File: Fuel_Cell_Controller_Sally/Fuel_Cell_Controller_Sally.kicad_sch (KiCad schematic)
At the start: 87 parts, among them J1 STM32-Prog-Header, J4 USB_C_Receptacle_USB2.0_14P, J6 OLED, Q1 SI2302A-TPMSCT-ND, Q2 SI2302A-TPMSCT-ND, SW1 PTS815 SJM 250 SMTR LFS, SW2 PTS815 SJM 250 SMTR LFS, U1 TPS259631, U2 AZ1117IH-3.3, U20 STM32G491CETx, U3 TPS565208, U4 TPS259631, U8 MCP6007, U9 USBLC6-2SC6, X2 OXETDLJANF-8MHZ

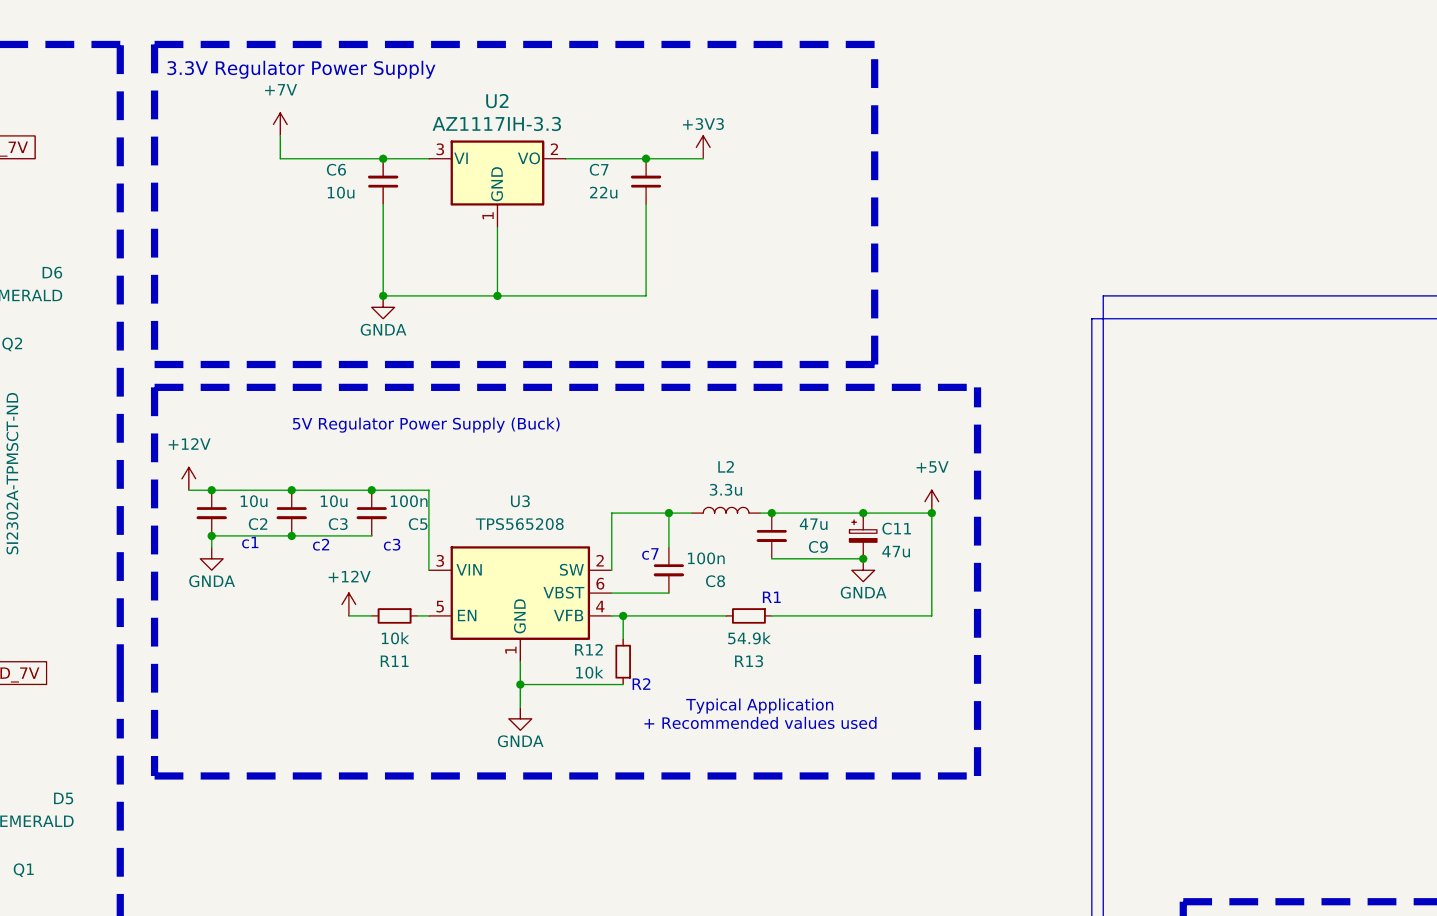
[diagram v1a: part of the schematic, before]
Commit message: FC con, power layout
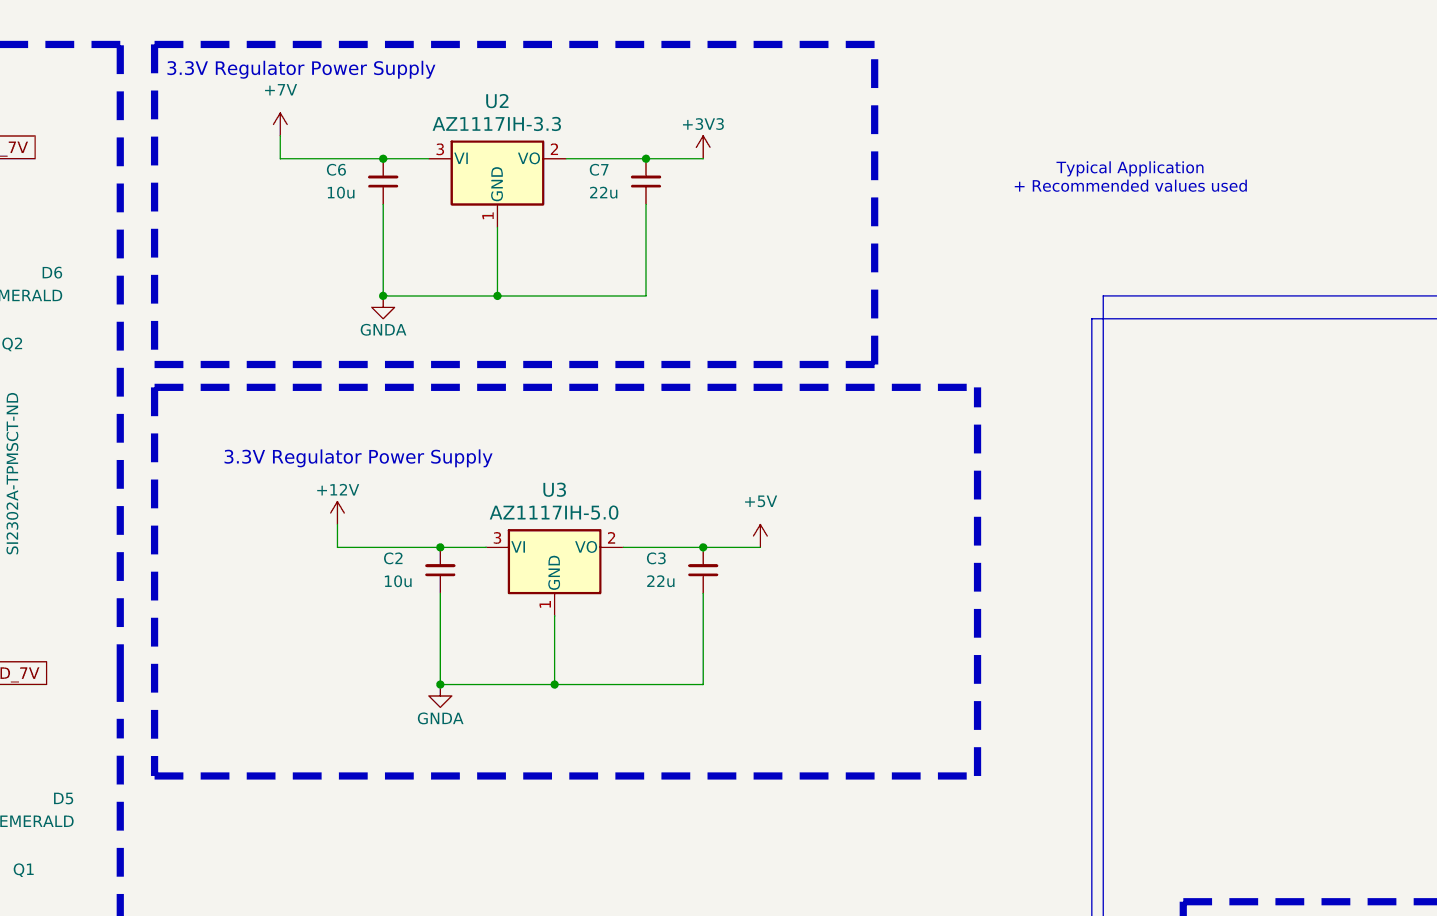
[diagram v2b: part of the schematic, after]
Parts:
- removed C11: 47u, Capacitor_SMD:CP_Elec_4x5.4, symbol Device:C_Polarized_Small
- removed C5, C8: 100n, Capacitor_SMD:C_0603_1608Metric, symbol Device:C_Small
- removed C9: 47u, Capacitor_SMD:C_0603_1608Metric, symbol Device:C_Small
- removed L2: 3.3u, Inductor_SMD:L_0805_2012Metric, symbol Device:L
- removed R11, R12: 10k, Resistor_SMD:R_0603_1608Metric, symbol Device:R_Small
- removed R13: 54.9k, Resistor_SMD:R_0603_1608Metric, symbol Device:R_Small
- removed U3: TPS565208, Package_TO_SOT_SMD:SOT-23-6, symbol Regulator_Switching:TPS565208
- added U3: AZ1117IH-5.0, Package_TO_SOT_SMD:SOT-223-3_TabPin2, symbol ecocad_lib_symbols:AZ1117IH-5.0
- C2: Part# C14663 -> C15849
- C3: value 10u -> 22u; Part# C14663 -> C15849
- X2: value OXETDLJANF-8MHZ -> OXETDLJANF-8MHZ
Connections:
- net +12V: now also C2.2, U3.3 (VI); no longer C2.1, C3.1
- net +5V: now also C3.2, U3.2 (VO)
- net GNDA: now also C2.1, C3.1, U3.1 (GND); no longer C2.2, C3.2
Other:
- note removed: "5V Regulator Power Supply (Buck)"
- note removed: "R1"
- note removed: "R2"
- note removed: "c1"
- note removed: "c2"
- note removed: "c3"
- note removed: "c7"

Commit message: MCU pinout layout in progress
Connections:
- net +3.3V is gone; now on net +3V3: C9.1, RV1.3, RV2.3, X2.1 (Tri-State), X2.4 (VDD)
- net BOOT0: no longer J6.3 (Pin_3), R25.1, U20.39 (PA15)
- new net I2C_{SCL}: J6.3 (Pin_3), R25.1, U20.39 (PA15)
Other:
- moved on the sheet: J4, U9
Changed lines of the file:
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@@
 	)
 	(junction
-		(at 252.73 182.88)
+		(at 245.11 182.88)
 		(diameter 0)
 		(color 0 0 0 0)
@@
 	)
 	(junction
-		(at 252.73 180.34)
+		(at 245.11 180.34)
 		(diameter 0)
 		(color 0 0 0 0)
 	)
 	(junction
-		(at 269.24 205.74)
+		(at 261.62 205.74)
 		(diameter 0)
 		(color 0 0 0 0)
@@
 	)
 	(no_connect
-		(at 254 170.18)
+		(at 246.38 170.18)
 	)
 	(no_connect
@@
 	)
 	(no_connect
-		(at 254 172.72)
+		(at 246.38 172.72)
 	)
 	(no_connect
@@
 	(wire
 		(pts
-			(xy 252.73 182.88) (xy 254 182.88)
+			(xy 245.11 182.88) (xy 246.38 182.88)
 		)
 		(stroke
@@
 	(wire
 		(pts
-			(xy 246.38 165.1) (xy 246.38 175.26)
+			(xy 238.76 165.1) (xy 238.76 175.26)
 		)
 		(stroke
@@
 	(wire
 		(pts
-			(xy 252.73 185.42) (xy 254 185.42)
+			(xy 245.11 185.42) (xy 246.38 185.42)
 		)
 		(stroke
@@
 	(wire
 		(pts
-			(xy 252.73 180.34) (xy 254 180.34)
+			(xy 245.11 180.34) (xy 246.38 180.34)
 		)
 		(stroke
@@
 	(wire
 		(pts
-			(xy 276.86 205.74) (xy 276.86 203.2)
+			(xy 269.24 205.74) (xy 269.24 203.2)
 		)
 		(stroke
@@
 	(wire
 		(pts
-			(xy 251.46 180.34) (xy 252.73 180.34)
+			(xy 243.84 180.34) (xy 245.11 180.34)
 		)
 		(stroke
@@
 	(wire
 		(pts
-			(xy 254 165.1) (xy 246.38 165.1)
+			(xy 246.38 165.1) (xy 238.76 165.1)
 		)
 		(stroke
@@
 	(wire
 		(pts
-			(xy 233.68 180.34) (xy 241.3 180.34)
+			(xy 226.06 180.34) (xy 233.68 180.34)
 		)
 		(stroke
@@
 	(wire
 		(pts
-			(xy 251.46 182.88) (xy 252.73 182.88)
+			(xy 243.84 182.88) (xy 245.11 182.88)
 		)
 		(stroke
@@
 	(wire
 		(pts
-			(xy 252.73 177.8) (xy 254 177.8)
+			(xy 245.11 177.8) (xy 246.38 177.8)
 		)
 		(stroke
@@
 	(wire
 		(pts
-			(xy 246.38 187.96) (xy 246.38 205.74)
+			(xy 238.76 187.96) (xy 238.76 205.74)
 		)
 		(stroke
@@
 	(wire
 		(pts
-			(xy 269.24 203.2) (xy 269.24 205.74)
+			(xy 261.62 203.2) (xy 261.62 205.74)
 		)
 		(stroke
@@
 	(wire
 		(pts
-			(xy 269.24 205.74) (xy 276.86 205.74)
+			(xy 261.62 205.74) (xy 269.24 205.74)
 		)
 		(stroke
@@
 	(wire
 		(pts
-			(xy 233.68 182.88) (xy 241.3 182.88)
+			(xy 226.06 182.88) (xy 233.68 182.88)
 		)
 		(stroke
@@
 	(wire
 		(pts
-			(xy 252.73 182.88) (xy 252.73 185.42)
+			(xy 245.11 182.88) (xy 245.11 185.42)
 		)
 		(stroke
@@
 	(wire
 		(pts
-			(xy 269.24 205.74) (xy 269.24 208.28)
+			(xy 261.62 205.74) (xy 261.62 208.28)
 		)
 		(stroke
@@
 	(wire
 		(pts
-			(xy 252.73 180.34) (xy 252.73 177.8)
+			(xy 245.11 180.34) (xy 245.11 177.8)
 		)
 		(stroke
@@
 	(wire
 		(pts
-			(xy 246.38 205.74) (xy 269.24 205.74)
+			(xy 238.76 205.74) (xy 261.62 205.74)
 		)
 		(stroke
@@
 	)
 	(rectangle
-		(start 228.6 154.94)
-		(end 312.42 214.63)
+		(start 220.98 154.94)
+		(end 304.8 214.63)
 		(stroke
 			(width 0.7874)
@@
 	(text "USB C\n"
 		(exclude_from_sim no)
-		(at 232.41 159.258 0)
+		(at 224.79 159.258 0)
 		(effects
 			(font
@@
 	)
 	(label "USB_{DP}"
-		(at 233.68 182.88 0)
+		(at 226.06 182.88 0)
 		(fields_autoplaced yes)
 		(effects
@@
 	)
 	(label "USB_{DM}"
-		(at 233.68 180.34 0)
+		(at 226.06 180.34 0)
 		(fields_autoplaced yes)
 		(effects
@@
 	)
 	(label "VBUS"
-		(at 246.38 165.1 0)
+		(at 238.76 165.1 0)
 		(fields_autoplaced yes)
 		(effects
@@
 		)
 	)
-	(label "PB8"
+	(label "PA15"
 		(at 379.73 233.68 0)
 		(fields_autoplaced yes)
@@
 			)
 		)
-		(property "Value" "+3.3V"
+		(property "Value" "+3V3"
 			(at 288.29 121.92 0)
 			(effects
@@
 	(symbol
 		(lib_id "power:GNDA")
-		(at 269.24 208.28 0)
+		(at 261.62 208.28 0)
 		(unit 1)
 		(exclude_from_sim no)
@@
 		(fields_autoplaced yes)
 		(property "Reference" "#PWR046"
-			(at 269.24 214.63 0)
+			(at 261.62 214.63 0)
 			(effects
 				(font
@@
 		)
 		(property "Value" "GNDA"
-			(at 269.24 213.36 0)
+			(at 261.62 213.36 0)
 			(effects
 				(font
@@
 		)
 		(property "Footprint" ""
-			(at 269.24 208.28 0)
+			(at 261.62 208.28 0)
 			(effects
 				(font
@@
 		)
 		(property "Datasheet" ""
-			(at 269.24 208.28 0)
+			(at 261.62 208.28 0)
 			(effects
 				(font
@@
 		)
 		(property "Description" ""
-			(at 269.24 208.28 0)
+			(at 261.62 208.28 0)
 			(effects
 				(font
@@
 			)
 		)
-		(property "Value" "+3.3V"
+		(property "Value" "+3V3"
 			(at 320.04 121.92 0)
 			(effects
@@
 	)
 	(symbol
+		(lib_id "power:+3V3")
+		(at 34.29 166.37 0)
+		(unit 1)
+		(exclude_from_sim no)
+		(in_bom yes)
+		(on_board yes)
+		(dnp no)
+		(fields_autoplaced yes)
+		(property "Reference" "#PWR026"
+			(at 34.29 170.18 0)
+			(effects
+				(font
+					(size 1.27 1.27)
+				)
+				(hide yes)
+			)
+		)
+		(property "Value" "+3V3"
+			(at 34.29 162.56 0)
+			(effects
+				(font
+					(size 1.27 1.27)
+				)
+			)
+		)
+		(property "Footprint" ""
+			(at 34.29 166.37 0)
+			(effects
+				(font
+					(size 1.27 1.27)
+				)
+				(hide yes)
+			)
+		)
+		(property "Datasheet" ""
+			(at 34.29 166.37 0)
+			(effects
+				(font
+					(size 1.27 1.27)
+				)
+				(hide yes)
+			)
+		)
+		(property "Description" ""
+			(at 34.29 166.37 0)
+			(effects
+				(font
+					(size 1.27 1.27)
+				)
+				(hide yes)
+			)
+		)
+		(pin "1"
+		)
+		(instances
+			(project "Fuel_Cell_Controller_Sally"
+				(path "/f651cec9-411c-4a4e-a163-5c49adbe6a12"
+					(reference "#PWR026")
+					(unit 1)
+				)
+			)
+		)
+	)
+	(symbol
 		(lib_id "power:GNDA")
 		(at 198.12 200.66 0)
@@
 	(symbol
 		(lib_id "Connector:USB_C_Receptacle_USB2.0_14P")
-		(at 269.24 180.34 0)
+		(at 261.62 180.34 0)
 		(mirror y)
 		(unit 1)
@@
 		(fields_autoplaced yes)
 		(property "Reference" "J4"
-			(at 280.67 179.0699 0)
+			(at 273.05 179.0699 0)
 			(effects
 				(font
@@
 		)
 		(property "Value" "USB_C_Receptacle_USB2.0_14P"
-			(at 280.67 181.6099 0)
+			(at 273.05 181.6099 0)
 			(effects
 				(font
@@
 		)
 		(property "Footprint" "Connector_USB:USB_C_Receptacle_GCT_USB4105-xx-A_16P_TopMnt_Horizontal"
-			(at 265.43 180.34 0)
+			(at 257.81 180.34 0)
 			(effects
 				(font
@@
 		)
 		(property "Datasheet" "https://www.usb.org/sites/default/files/documents/usb_type-c.zip"
-			(at 265.43 180.34 0)
+			(at 257.81 180.34 0)
 			(effects
 				(font
@@
 		)
 		(property "Description" "USB 2.0-only 14P Type-C Receptacle connector"
-			(at 269.24 180.34 0)
+			(at 261.62 180.34 0)
 			(effects
 				(font
@@
 	(symbol
 		(lib_id "Power_Protection:USBLC6-2SC6")
-		(at 246.38 180.34 0)
+		(at 238.76 180.34 0)
 		(mirror y)
 		(unit 1)
@@
 		(dnp no)
 		(property "Reference" "U9"
-			(at 244.7289 172.72 0)
+			(at 237.1089 172.72 0)
 			(effects
 				(font
@@
 		)
 		(property "Value" "USBLC6-2SC6"
-			(at 244.7289 175.26 0)
+			(at 237.1089 175.26 0)
 			(effects
 				(font
@@
 		)
 		(property "Footprint" "Package_TO_SOT_SMD:SOT-23-6"
-			(at 245.11 186.69 0)
+			(at 237.49 186.69 0)
 			(effects
 				(font
@@
 		)
 		(property "Datasheet" "https://www.st.com/resource/en/datasheet/usblc6-2.pdf"
-			(at 245.11 188.595 0)
+			(at 237.49 188.595 0)
 			(effects
 				(font
@@
 		)
 		(property "Description" "Very low capacitance ESD protection diode, 2 data-line, SOT-23-6"
-			(at 246.38 180.34 0)
+			(at 238.76 180.34 0)
 			(effects
 				(font
@@
 					(unit 1)
 				)
-			)
-		)
-	)
-	(symbol
-		(lib_id "power:+3.3V")
-		(at 34.29 166.37 0)
-		(unit 1)
-		(exclude_from_sim no)
-		(in_bom yes)
-		(on_board yes)
-		(dnp no)
-		(fields_autoplaced yes)
-		(property "Reference" "#PWR0118"
-			(at 34.29 170.18 0)
-			(effects
-				(font
-					(size 1.27 1.27)
-				)
-				(hide yes)
-			)
-		)
-		(property "Value" "+3.3V"
-			(at 34.29 161.29 0)
-			(effects
-				(font
-					(size 1.27 1.27)
-				)
-			)
-		)
-		(property "Footprint" ""
-			(at 34.29 166.37 0)
-			(effects
-				(font
-					(size 1.27 1.27)
-				)
-				(hide yes)
-			)
-		)
-		(property "Datasheet" ""
-			(at 34.29 166.37 0)
-			(effects
-				(font
-					(size 1.27 1.27)
-				)
-				(hide yes)
-			)
-		)
-		(property "Description" "Power symbol creates a global label with name \"+3.3V\""
-			(at 34.29 166.37 0)
-			(effects
-				(font
-					(size 1.27 1.27)
-				)
-				(hide yes)
-			)
-		)
-		(pin "1"
-		)
-		(instances
-			(project "Fuel_Cell_Controller_Prototype"
-				(path "/f651cec9-411c-4a4e-a163-5c49adbe6a12"
-					(reference "#PWR0118")
-					(unit 1)
-				)

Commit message: layout
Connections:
- net EXT_{STOP} renamed PA0
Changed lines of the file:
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@@
-		)
-	)
-	(label "EXT_{STOP}"
-		(at 161.29 189.23 180)
-		(fields_autoplaced yes)
-		(effects
-			(font
-				(size 1.27 1.27)
-			)
-			(justify right bottom)
 		)
 	)

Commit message: Complete first Rev
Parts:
- added C8: 100n, Capacitor_SMD:C_0402_1005Metric, symbol Device:C_Small
- H1, H2, H3, H4: footprint MountingHole:MountingHole_3.2mm_M3 -> MountingHole:MountingHole_3.2mm_M3_DIN965_Pad
- J6: footprint Connector_PinSocket_2.54mm:PinSocket_1x04_P2.54mm_Vertical -> ecocad_lib_footprints:Display_128x64_096_I2C
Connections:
- net +3V3: now also C8.1; no longer C21.1, C22.1, FB1.2, U20.21 (VDDA)
- net GNDA: now also C8.2
- new net: C21.1, C22.1, FB1.2, U20.21 (VDDA)
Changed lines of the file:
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@@
 	)
 	(junction
+		(at 95.25 173.99)
+		(diameter 0)
+		(color 0 0 0 0)
+	)
+	(junction
 		(at 132.08 31.75)
 		(diameter 0)
@@
 	)
 	(junction
-		(at 130.81 181.61)
+		(at 128.27 181.61)
 		(diameter 0)
 		(color 0 0 0 0)
 	)
 	(junction
-		(at 128.27 181.61)
+		(at 48.26 35.56)
 		(diameter 0)
 		(color 0 0 0 0)
 	)
 	(junction
-		(at 48.26 35.56)
+		(at 372.11 124.46)
 		(diameter 0)
 		(color 0 0 0 0)
 	)
 	(junction
-		(at 372.11 124.46)
+		(at 102.87 163.83)
 		(diameter 0)
 		(color 0 0 0 0)
@@
 	)
 	(junction
-		(at 110.49 181.61)
-		(diameter 0)
-		(color 0 0 0 0)
-	)
-	(junction
 		(at 46.99 92.71)
 		(diameter 0)
@@
 	(wire
 		(pts
-			(xy 104.14 163.83) (xy 104.14 181.61)
+			(xy 123.19 163.83) (xy 123.19 181.61)
 		)
 		(stroke
@@
 		)
 	)
-	(wire
-		(pts
-			(xy 128.27 163.83) (xy 128.27 181.61)
-		)
-		(stroke
-			(width 0)
-			(type default)
-		)
-	)
 	(polyline
 		(pts
@@
 	(wire
 		(pts
-			(xy 186.69 72.39) (xy 198.12 72.39)
+			(xy 132.08 163.83) (xy 132.08 176.53)
 		)
 		(stroke
@@
 	(wire
 		(pts
-			(xy 133.35 181.61) (xy 130.81 181.61)
+			(xy 186.69 72.39) (xy 198.12 72.39)
 		)
 		(stroke
@@
 	(wire
 		(pts
+			(xy 104.14 163.83) (xy 123.19 163.83)
+		)
+		(stroke
+			(width 0)
+			(type default)
+		)
+	)
+	(wire
+		(pts
 			(xy 335.28 195.58) (xy 335.28 199.39)
 		)
@@
 	(wire
 		(pts
-			(xy 95.25 163.83) (xy 104.14 163.83)
+			(xy 95.25 163.83) (xy 102.87 163.83)
 		)
 		(stroke
@@
 	(wire
 		(pts
+			(xy 102.87 163.83) (xy 104.14 163.83)
+		)
+		(stroke
+			(width 0)
+			(type default)
+		)
+	)
+	(wire
+		(pts
 			(xy 144.78 31.75) (xy 144.78 33.02)
 		)
@@
 	(wire
 		(pts
+			(xy 102.87 163.83) (xy 102.87 166.37)
+		)
+		(stroke
+			(width 0)
+			(type default)
+		)
+	)
+	(wire
+		(pts
 			(xy 80.01 242.57) (xy 110.49 242.57)
 		)
@@
 	(wire
 		(pts
-			(xy 104.14 181.61) (xy 110.49 181.61)
-		)
-		(stroke
-			(width 0)
-			(type default)
-		)
-	)
-	(wire
-		(pts
 			(xy 163.83 209.55) (xy 163.83 210.82)
 		)
@@
 	(wire
 		(pts
+			(xy 102.87 173.99) (xy 95.25 173.99)
+		)
+		(stroke
+			(width 0)
+			(type default)
+		)
+	)
+	(wire
+		(pts
 			(xy 46.99 100.33) (xy 46.99 102.87)
 		)
@@
 	(wire
 		(pts
+			(xy 132.08 176.53) (xy 133.35 176.53)
+		)
+		(stroke
+			(width 0)
+			(type default)
+		)
+	)
+	(wire
+		(pts
 			(xy 39.37 35.56) (xy 48.26 35.56)
 		)
@@
 	(wire
 		(pts
-			(xy 133.35 184.15) (xy 133.35 181.61)
+			(xy 133.35 176.53) (xy 133.35 184.15)
+		)
+		(stroke
+			(width 0)
+			(type default)
+		)
+	)
+	(wire
+		(pts
+			(xy 102.87 171.45) (xy 102.87 173.99)
 		)
 		(stroke
@@
 	(wire
 		(pts
-			(xy 128.27 163.83) (xy 134.62 163.83)
+			(xy 132.08 163.83) (xy 134.62 163.83)
 		)
 		(stroke
@@
 			)
 		)
-		(property "Footprint" "MountingHole:MountingHole_3.2mm_M3"
+		(property "Footprint" "MountingHole:MountingHole_3.2mm_M3_DIN965_Pad"
 			(at 261.62 271.78 0)
 			(effects
@@
 			)
 		)
-		(property "Footprint" "MountingHole:MountingHole_3.2mm_M3"
+		(property "Footprint" "MountingHole:MountingHole_3.2mm_M3_DIN965_Pad"
 			(at 280.67 278.13 0)
 			(effects
@@
 			)
 		)
-		(property "Footprint" "Connector_PinSocket_2.54mm:PinSocket_1x04_P2.54mm_Vertical"
+		(property "Footprint" "ecocad_lib_footprints:Display_128x64_096_I2C"
 			(at 389.89 236.22 0)
 			(effects
@@
 	(symbol
 		(lib_id "Device:C_Small")
+		(at 102.87 168.91 0)
+		(unit 1)
+		(exclude_from_sim no)
+		(in_bom yes)
+		(on_board yes)
+		(dnp no)
+		(property "Reference" "C8"
+			(at 104.14 166.37 0)
+			(effects
+				(font
+					(size 1.27 1.27)
+				)
+				(justify left)
+			)
+		)
+		(property "Value" "100n"
+			(at 109.22 171.45 0)
+			(effects
+				(font
+					(size 1.27 1.27)
+				)
+				(justify right)
+			)
+		)
+		(property "Footprint" "Capacitor_SMD:C_0402_1005Metric"
+			(at 102.87 168.91 0)
+			(effects
+				(font
+					(size 1.27 1.27)
+				)
+				(hide yes)
+			)
+		)
+		(property "Datasheet" "https://datasheet.lcsc.com/lcsc/2304140030_FH--Guangdong-Fenghua-Advanced-Tech-0603B104K101NT_C88219.pdf"
+			(at 102.87 168.91 0)
+			(effects
+				(font
+					(size 1.27 1.27)
+				)
+				(hide yes)
+			)
+		)
+		(property "Description" ""
+			(at 102.87 168.91 0)
+			(effects
+				(font
+					(size 1.27 1.27)
+				)
+				(hide yes)
+			)
+		)
+		(property "Part#" "C1525"
+			(at 102.87 168.91 0)
+			(effects
+				(font
+					(size 1.27 1.27)
+				)
+				(hide yes)
+			)
+		)
+		(pin "1"
+		)
+		(pin "2"
+		)
+		(instances
+			(project "Fuel_Cell_Controller_Sally"
+				(path "/f651cec9-411c-4a4e-a163-5c49adbe6a12"
+					(reference "C8")
+					(unit 1)
+				)
+			)
+		)
+	)
+	(symbol
+		(lib_id "Device:C_Small")
 		(at 35.56 270.51 0)
 		(unit 1)
@@
 			)
 		)
-		(property "Footprint" "MountingHole:MountingHole_3.2mm_M3"
+		(property "Footprint" "MountingHole:MountingHole_3.2mm_M3_DIN965_Pad"
 			(at 280.67 271.78 0)
 			(effects
@@
 			)
 		)
-		(property "Footprint" "MountingHole:MountingHole_3.2mm_M3"
+		(property "Footprint" "MountingHole:MountingHole_3.2mm_M3_DIN965_Pad"
 			(at 261.62 278.13 0)
 			(effects

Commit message: $
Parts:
- removed R25 (x2): 10k, Resistor_SMD:R_0603_1608Metric, symbol Device:R_Small
- C11: value 2u2 -> 1u
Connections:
- net +3V3: no longer R25.2, R25.2
- net BTN_{1}: now also R25.2; no longer R25.1
- net BTN_{2}: now also R25.2; no longer R25.1
- net GNDA: no longer J1.5 (GND), J1.6 (GND)
- net at C11.1: now also R25.1 (x2)
- new net GND: J1.5 (GND), J1.6 (GND)
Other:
- note added: "5V Regulator Power Supply"
- note added: "MCU Pullup"
- note added: "τ = 10ms f_{c} = 16Hz"
- note removed: "τ = 30ms"
- moved on the sheet: C11, C12, C19, C20, C8, R25, SW1

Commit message: update
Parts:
- removed H2, H3, H4: MountingHole, MountingHole:MountingHole_3.2mm_M3_DIN965_Pad, symbol Mechanical:MountingHole
- added H102, H103, H104: MountingHole, MountingHole:MountingHole_3.5mm, symbol Mechanical:MountingHole
- added R115, R117: 30k, Resistor_SMD:R_0603_1608Metric, symbol Device:R_Small
- H101: renamed from H1; footprint MountingHole:MountingHole_3.2mm_M3_DIN965_Pad -> MountingHole:MountingHole_3.5mm
- R114: renamed from R15; value 100k -> 12k
- R116: renamed from R14; value 100k -> 12k
- renumbered C17 to C105, C16 to C106, C46 to C108, C47 to C109, C8 to C112, C19 to C113, C6 to C116, C2 to C117, C7 to C118, C3 to C119, C23 to C120, D1 to D101, D2 to D102, D6 to D103, D5 to D104, D15 to D105, D16 to D106, D10 to D107, D17 to D108, D3 to D109, D4 to D110, J4 to J101, J1 to J102, Q2 to Q101, Q1 to Q102, R2 to R103, R3 to R104, R7 to R106, R6 to R107, R57 to R108, R4 to R109, R5 to R110, R8 to R111, R9 to R112, R10 to R113, R17 to R118, R16 to R119, R54 to R122, R55 to R123, R53 to R124, R56 to R125, RV1 to RV101, RV2 to RV102, TP1 to TP101, U4 to U101, U1 to U102, U20 to U103, U2 to U104, U3 to U105, U9 to U106, U8 to U107, X2 to X101
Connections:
- net FLT_{12}: now also R115.2
- net FLT_{7}: now also R117.2
- net GNDA: now also R115.1, R117.1
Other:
- moved on the sheet: C117, C119, U105
